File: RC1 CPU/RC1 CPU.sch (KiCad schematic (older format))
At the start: 47 parts, among them J1 Expansion, J2 RC1_UI_Port, J3 BARREL_JACK, M1 Mounting, M2 Mounting, M3 Mounting, M4 Mounting, U1 WD65C02, U2 HM62256BLP-7, U3 28C256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

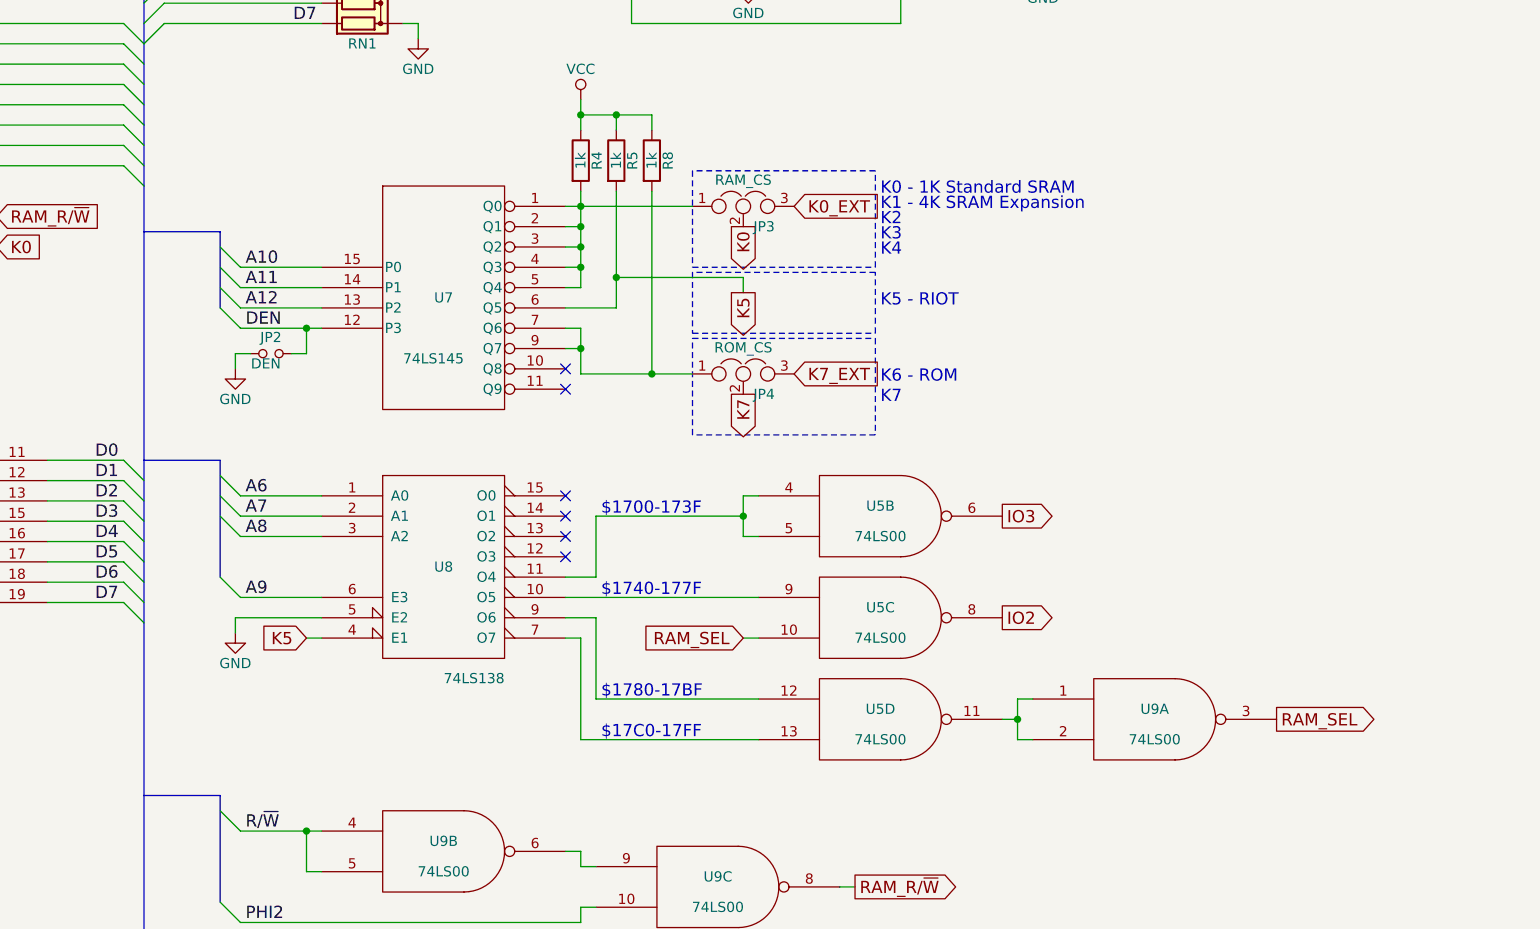
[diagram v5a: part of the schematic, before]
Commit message: Added 65K expansion notice to CPU schematic
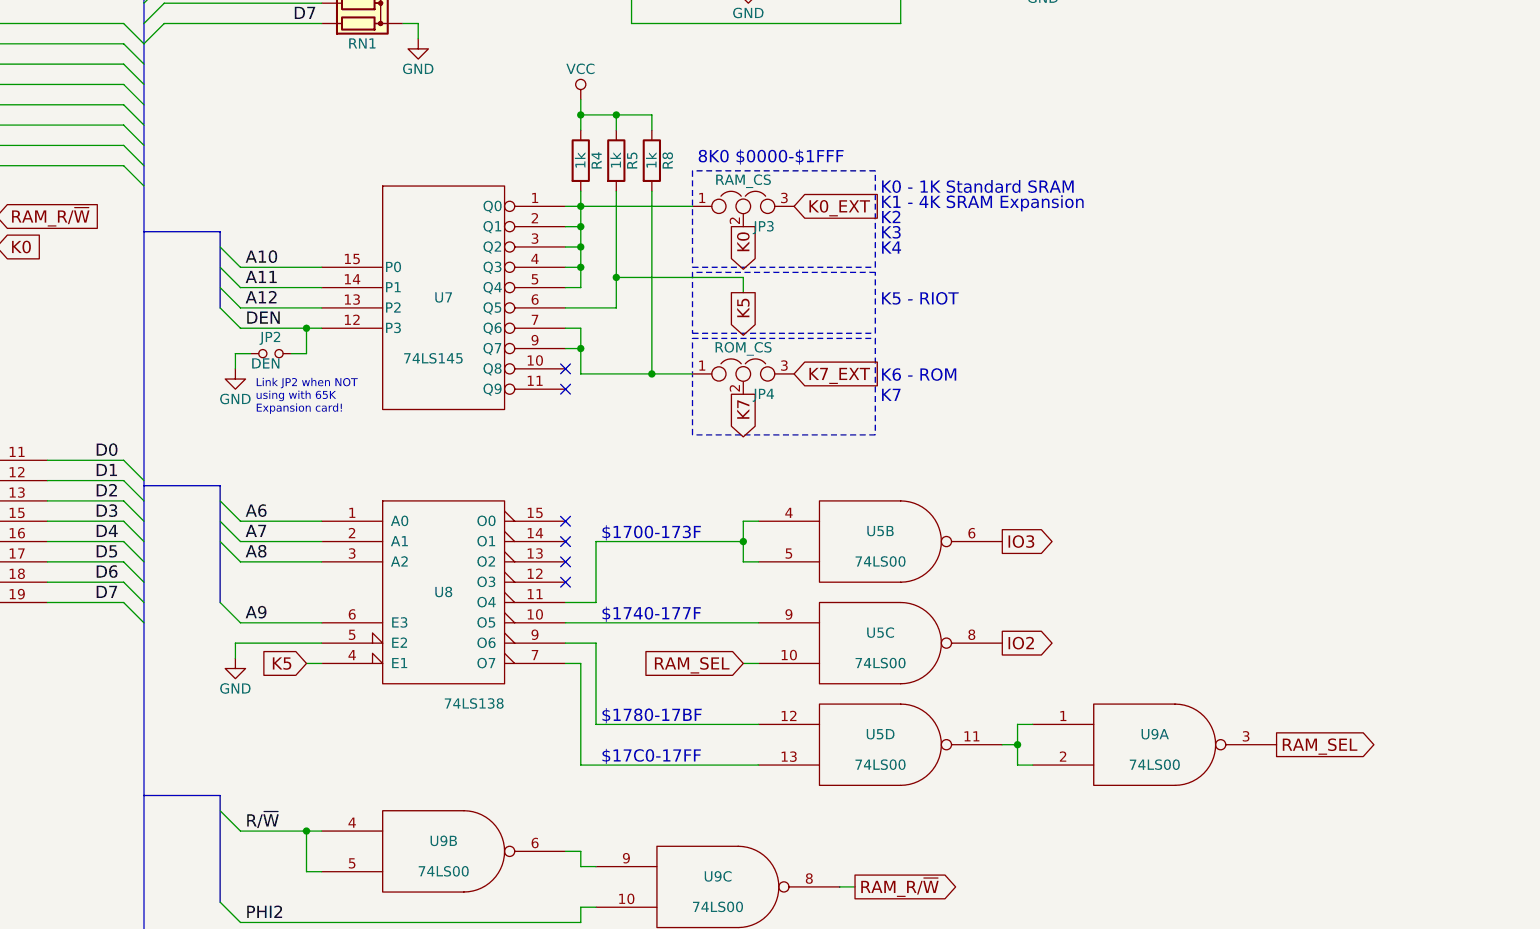
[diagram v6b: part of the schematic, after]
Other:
- note added: "8K0 $0000-$1FFF"
- note added: "Link JP2 when NOT\nusing with 65K\nExpansion card!"
- moved on the sheet: U5B, U5C, U5D, U8, U9A
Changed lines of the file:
@@
 L 74LS138 U8
 U 1 1 5D6D4F15
-P 5425 6600
-F 0 "U8" H 5425 6600 50  0000 C CNN
-F 1 "74LS138" H 5575 6051 50  0000 C CNN
-F 2 "Housings_DIP:DIP-16_W7.62mm_Socket" H 5425 6600 50  0001 C CNN
-F 3 "" H 5425 6600 50  0001 C CNN
-	1    5425 6600
-	1    0    0    -1
-$EndComp
-Text GLabel 4750 6950 0    60   Input ~ 0
+P 5425 6725
+F 0 "U8" H 5425 6725 50  0000 C CNN
+F 1 "74LS138" H 5575 6176 50  0000 C CNN
+F 2 "Housings_DIP:DIP-16_W7.62mm_Socket" H 5425 6725 50  0001 C CNN
+F 3 "" H 5425 6725 50  0001 C CNN
+	1    5425 6725
+	1    0    0    -1
+$EndComp
+Text GLabel 4750 7075 0    60   Input ~ 0
 K5
-Text Label 4450 6450 0    60   ~ 0
+Text Label 4450 6575 0    60   ~ 0
 A8
 Entry Wire Line
-	4325 6350 4425 6450
-Text Label 4450 6350 0    60   ~ 0
+	4325 6475 4425 6575
+Text Label 4450 6475 0    60   ~ 0
 A7
 Entry Wire Line
-	4325 6250 4425 6350
-Entry Wire Line
-	4325 6650 4425 6750
-Text Label 4450 6750 0    60   ~ 0
+	4325 6375 4425 6475
+Entry Wire Line
+	4325 6775 4425 6875
+Text Label 4450 6875 0    60   ~ 0
 A9
 $Comp
 L GND #PWR025
 U 1 1 5D6D7527
-P 4400 6925
-F 0 "#PWR025" H 4400 6675 50  0001 C CNN
-F 1 "GND" H 4400 6775 50  0000 C CNN
-F 2 "" H 4400 6925 50  0001 C CNN
-F 3 "" H 4400 6925 50  0001 C CNN
-	1    4400 6925
-	1    0    0    -1
-$EndComp
-NoConn ~ 6025 6550
-NoConn ~ 6025 6450
-NoConn ~ 6025 6350
-NoConn ~ 6025 6250
+P 4400 7050
+F 0 "#PWR025" H 4400 6800 50  0001 C CNN
+F 1 "GND" H 4400 6900 50  0000 C CNN
+F 2 "" H 4400 7050 50  0001 C CNN
+F 3 "" H 4400 7050 50  0001 C CNN
+	1    4400 7050
+	1    0    0    -1
+$EndComp
+NoConn ~ 6025 6675
+NoConn ~ 6025 6575
+NoConn ~ 6025 6475
+NoConn ~ 6025 6375
 $Comp
 L 74LS00 U5
 U 2 1 5D6D964C
-P 7575 6350
-F 0 "U5" H 7575 6400 50  0000 C CNN
-F 1 "74LS00" H 7575 6250 50  0000 C CNN
-F 2 "Housings_DIP:DIP-14_W7.62mm_Socket" H 7575 6350 50  0001 C CNN
-F 3 "" H 7575 6350 50  0001 C CNN
-	2    7575 6350
+P 7575 6475
+F 0 "U5" H 7575 6525 50  0000 C CNN
+F 1 "74LS00" H 7575 6375 50  0000 C CNN
+F 2 "Housings_DIP:DIP-14_W7.62mm_Socket" H 7575 6475 50  0001 C CNN
+F 3 "" H 7575 6475 50  0001 C CNN
+	2    7575 6475
 	1    0    0    -1
 $EndComp
@@
 L 74LS00 U5
 U 3 1 5D6D9A2F
-P 7575 6850
-F 0 "U5" H 7575 6900 50  0000 C CNN
-F 1 "74LS00" H 7575 6750 50  0000 C CNN
-F 2 "Housings_DIP:DIP-14_W7.62mm_Socket" H 7575 6850 50  0001 C CNN
-F 3 "" H 7575 6850 50  0001 C CNN
-	3    7575 6850
+P 7575 6975
+F 0 "U5" H 7575 7025 50  0000 C CNN
+F 1 "74LS00" H 7575 6875 50  0000 C CNN
+F 2 "Housings_DIP:DIP-14_W7.62mm_Socket" H 7575 6975 50  0001 C CNN
+F 3 "" H 7575 6975 50  0001 C CNN
+	3    7575 6975
 	1    0    0    -1
 $EndComp
@@
 L 74LS00 U5
 U 4 1 5D6DAB18
-P 7575 7350
-F 0 "U5" H 7575 7400 50  0000 C CNN
-F 1 "74LS00" H 7575 7250 50  0000 C CNN
-F 2 "Housings_DIP:DIP-14_W7.62mm_Socket" H 7575 7350 50  0001 C CNN
-F 3 "" H 7575 7350 50  0001 C CNN
-	4    7575 7350
+P 7575 7475
+F 0 "U5" H 7575 7525 50  0000 C CNN
+F 1 "74LS00" H 7575 7375 50  0000 C CNN
+F 2 "Housings_DIP:DIP-14_W7.62mm_Socket" H 7575 7475 50  0001 C CNN
+F 3 "" H 7575 7475 50  0001 C CNN
+	4    7575 7475
 	1    0    0    -1
 $EndComp
@@
 L 74LS00 U9
 U 1 1 5D6DB7A4
-P 8925 7350
-F 0 "U9" H 8925 7400 50  0000 C CNN
-F 1 "74LS00" H 8925 7250 50  0000 C CNN
-F 2 "Housings_DIP:DIP-14_W7.62mm_Socket" H 8925 7350 50  0001 C CNN
-F 3 "" H 8925 7350 50  0001 C CNN
-	1    8925 7350
-	1    0    0    -1
-$EndComp
-Text GLabel 8175 6350 2    60   Output ~ 0
+P 8925 7475
+F 0 "U9" H 8925 7525 50  0000 C CNN
+F 1 "74LS00" H 8925 7375 50  0000 C CNN
+F 2 "Housings_DIP:DIP-14_W7.62mm_Socket" H 8925 7475 50  0001 C CNN
+F 3 "" H 8925 7475 50  0001 C CNN
+	1    8925 7475
+	1    0    0    -1
+$EndComp
+Text GLabel 8175 6475 2    60   Output ~ 0
 IO3
-Text GLabel 8175 6850 2    60   Output ~ 0
+Text GLabel 8175 6975 2    60   Output ~ 0
 IO2
-Text GLabel 9525 7350 2    60   Output ~ 0
+Text GLabel 9525 7475 2    60   Output ~ 0
 RAM_SEL
 Text GLabel 4025 9375 2    60   Input ~ 0
@@
 Text Notes 7575 5000 0    60   ~ 0
 K3
-Text Label 4450 6250 0    60   ~ 0
+Text Label 4450 6375 0    60   ~ 0
 A6
 Entry Wire Line
-	4325 6150 4425 6250
-Text GLabel 6900 6950 0    60   Input ~ 0
+	4325 6275 4425 6375
+Text GLabel 6900 7075 0    60   Input ~ 0
 RAM_SEL
-Text Notes 6200 7450 0    60   ~ 0
+Text Notes 6200 7575 0    60   ~ 0
 $17C0-17FF
-Text Notes 6200 7250 0    60   ~ 0
+Text Notes 6200 7375 0    60   ~ 0
 $1780-17BF
-Text Notes 6200 6750 0    60   ~ 0
+Text Notes 6200 6875 0    60   ~ 0
 $1740-177F
-Text Notes 6200 6350 0    60   ~ 0
+Text Notes 6200 6475 0    60   ~ 0
 $1700-173F
 Text GLabel 15050 9750 0    60   Input ~ 0
@@
 	4325 4950 3950 4950
 Wire Wire Line
-	4750 6950 4825 6950
-Wire Wire Line
-	4425 6450 4825 6450
-Wire Wire Line
-	4425 6350 4825 6350
-Wire Wire Line
-	4425 6750 4825 6750
-Wire Wire Line
-	4400 6850 4825 6850
-Wire Wire Line
-	4400 6850 4400 6925
-Wire Bus Line
-	4325 6075 4325 6650
-Wire Wire Line
-	8175 7350 8250 7350
-Wire Wire Line
-	8250 7250 8250 7450
-Wire Wire Line
-	8250 7250 8325 7250
-Wire Wire Line
-	8250 7450 8325 7450
-Connection ~ 8250 7350
+	4750 7075 4825 7075
+Wire Wire Line
+	4425 6575 4825 6575
+Wire Wire Line
+	4425 6475 4825 6475
+Wire Wire Line
+	4425 6875 4825 6875
+Wire Wire Line
+	4400 6975 4825 6975
+Wire Wire Line
+	4400 6975 4400 7050
+Wire Bus Line
+	4325 6200 4325 6775
+Wire Wire Line
+	8175 7475 8250 7475
+Wire Wire Line
+	8250 7375 8250 7575
+Wire Wire Line
+	8250 7375 8325 7375
+Wire Wire Line
+	8250 7575 8325 7575
+Connection ~ 8250 7475
 Wire Wire Line
 	4025 9375 3425 9375
@@
 	6700 9375 6425 9375
 Wire Wire Line
-	4425 6250 4825 6250
-Wire Bus Line
-	4325 6075 3950 6075
-Wire Wire Line
-	6900 6450 6975 6450
-Wire Wire Line
-	6900 6250 6900 6450
-Wire Wire Line
-	6900 6250 6975 6250
-Wire Wire Line
-	6025 6650 6175 6650
-Connection ~ 6900 6350
-Wire Wire Line
-	6025 6750 6975 6750
-Wire Wire Line
-	6900 6950 6975 6950
-Wire Wire Line
-	6025 6950 6100 6950
-Wire Wire Line
-	6100 6950 6100 7450
-Wire Wire Line
-	6100 7450 6975 7450
-Wire Wire Line
-	6025 6850 6175 6850
-Wire Wire Line
-	6175 6850 6175 7250
-Wire Wire Line
-	6175 7250 6975 7250
-Wire Wire Line
-	6175 6650 6175 6350
-Wire Wire Line
-	6175 6350 6900 6350
+	4425 6375 4825 6375
+Wire Bus Line
+	4325 6200 3950 6200
+Wire Wire Line
+	6900 6575 6975 6575
+Wire Wire Line
+	6900 6375 6900 6575
+Wire Wire Line
+	6900 6375 6975 6375
+Wire Wire Line
+	6025 6775 6175 6775
+Connection ~ 6900 6475
+Wire Wire Line
+	6025 6875 6975 6875
+Wire Wire Line
+	6900 7075 6975 7075
+Wire Wire Line
+	6025 7075 6100 7075
+Wire Wire Line
+	6100 7075 6100 7575
+Wire Wire Line
+	6100 7575 6975 7575
+Wire Wire Line
+	6025 6975 6175 6975
+Wire Wire Line
+	6175 6975 6175 7375
+Wire Wire Line
+	6175 7375 6975 7375
+Wire Wire Line
+	6175 6775 6175 6475
+Wire Wire Line
+	6175 6475 6900 6475
 Wire Wire Line
 	6275 5175 6900 5175
@@
 Text Notes 7575 5700 0    60   ~ 0
 K6 - ROM
+Text Notes 6675 4625 0    60   ~ 0
+8K0 $0000-$1FFF
+Text Notes 4500 5850 0    39   ~ 0
+Link JP2 when NOT\nusing with 65K\nExpansion card!
 $EndSCHEMATC

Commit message: Eliminated 74LS145 from CPU module
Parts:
- removed R4, R5, R8: 1k, Resistors_THT:R_Axial_DIN0207_L6.3mm_D2.5mm_P10.16mm_Horizontal, symbol R
- removed U7: 74LS145, Housings_DIP:DIP-16_W7.62mm_Socket, symbol 74LS145
- added J4: K1-4, Pin_Headers:Pin_Header_Straight_1x04_Pitch2.54mm, symbol Conn_01x04
- added U7: 74LS138, Housings_DIP:DIP-16_W7.62mm_Socket, symbol 74LS138
- U1: value WD65C02 -> 6502; symbol WD65C02 -> 6502
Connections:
- net A10: now also U7.1 (A0)
- net A11: now also U7.2 (A1)
- net A12: now also U7.3 (A2)
- net DEN: now also U7.4 (E1), U7.5 (E2)
- net GND: now also U3.14 (GND), U7.8 (GND); no longer U9.12, U9.13
- net K5: now also U7.10 (O5)
- net VCC: now also U1.38 (~SO), U3.28 (VCC), U7.16 (VCC), U7.6 (E3)
- net at JP3.1: now also U7.15 (O0)
- net at JP4.1: now also U9.11
- net at U5.4, U5.5: now also U5.11; no longer U8.11 (O4)
- net W/~R: now reaches U9.6, U9.9
- net IO3 renamed ~IO3
- net ~IO3: now also U8.11 (O4); no longer U5.6
- net RAM_SEL renamed ~RAM_SEL
- net ~RAM_SEL: now also U5.6; no longer U9.3
- net TAPE: no longer names the net of J1.39 (P39)
- net TAPE: no longer J2.20 (P20)
- new net: U7.9 (O6), U9.1
- new net: U7.7 (O7), U9.2
- new net: U9.12, U9.13, U9.3
- new net: J4.4 (Pin_4), U7.11 (O4)
- new net: J4.3 (Pin_3), U7.12 (O3)
- new net: J4.2 (Pin_2), U7.13 (O2)
- new net: J4.1 (Pin_1), U7.14 (O1)
- no-connect marks 26 -> 22
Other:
- note added: "A"
- note added: "B"
- note added: "C"
- note added: "K0"
- note added: "K1"
- note added: "K5"
- note added: "K6"
- note added: "K6 - EEPROM (6530-003)"
- note added: "K7 - EEPROM (6530-002)"
- note removed: "K1 - 4K SRAM Expansion"
- note removed: "K6 - ROM"
- moved on the sheet: C1, C2, C3, C4, C5, C6, C7, C8, C9, JP1, JP2, JP3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
